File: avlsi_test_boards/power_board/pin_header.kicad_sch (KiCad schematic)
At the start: 3 parts, among them J5 Conn_01x02_Pin, J6 Conn_01x02_Pin

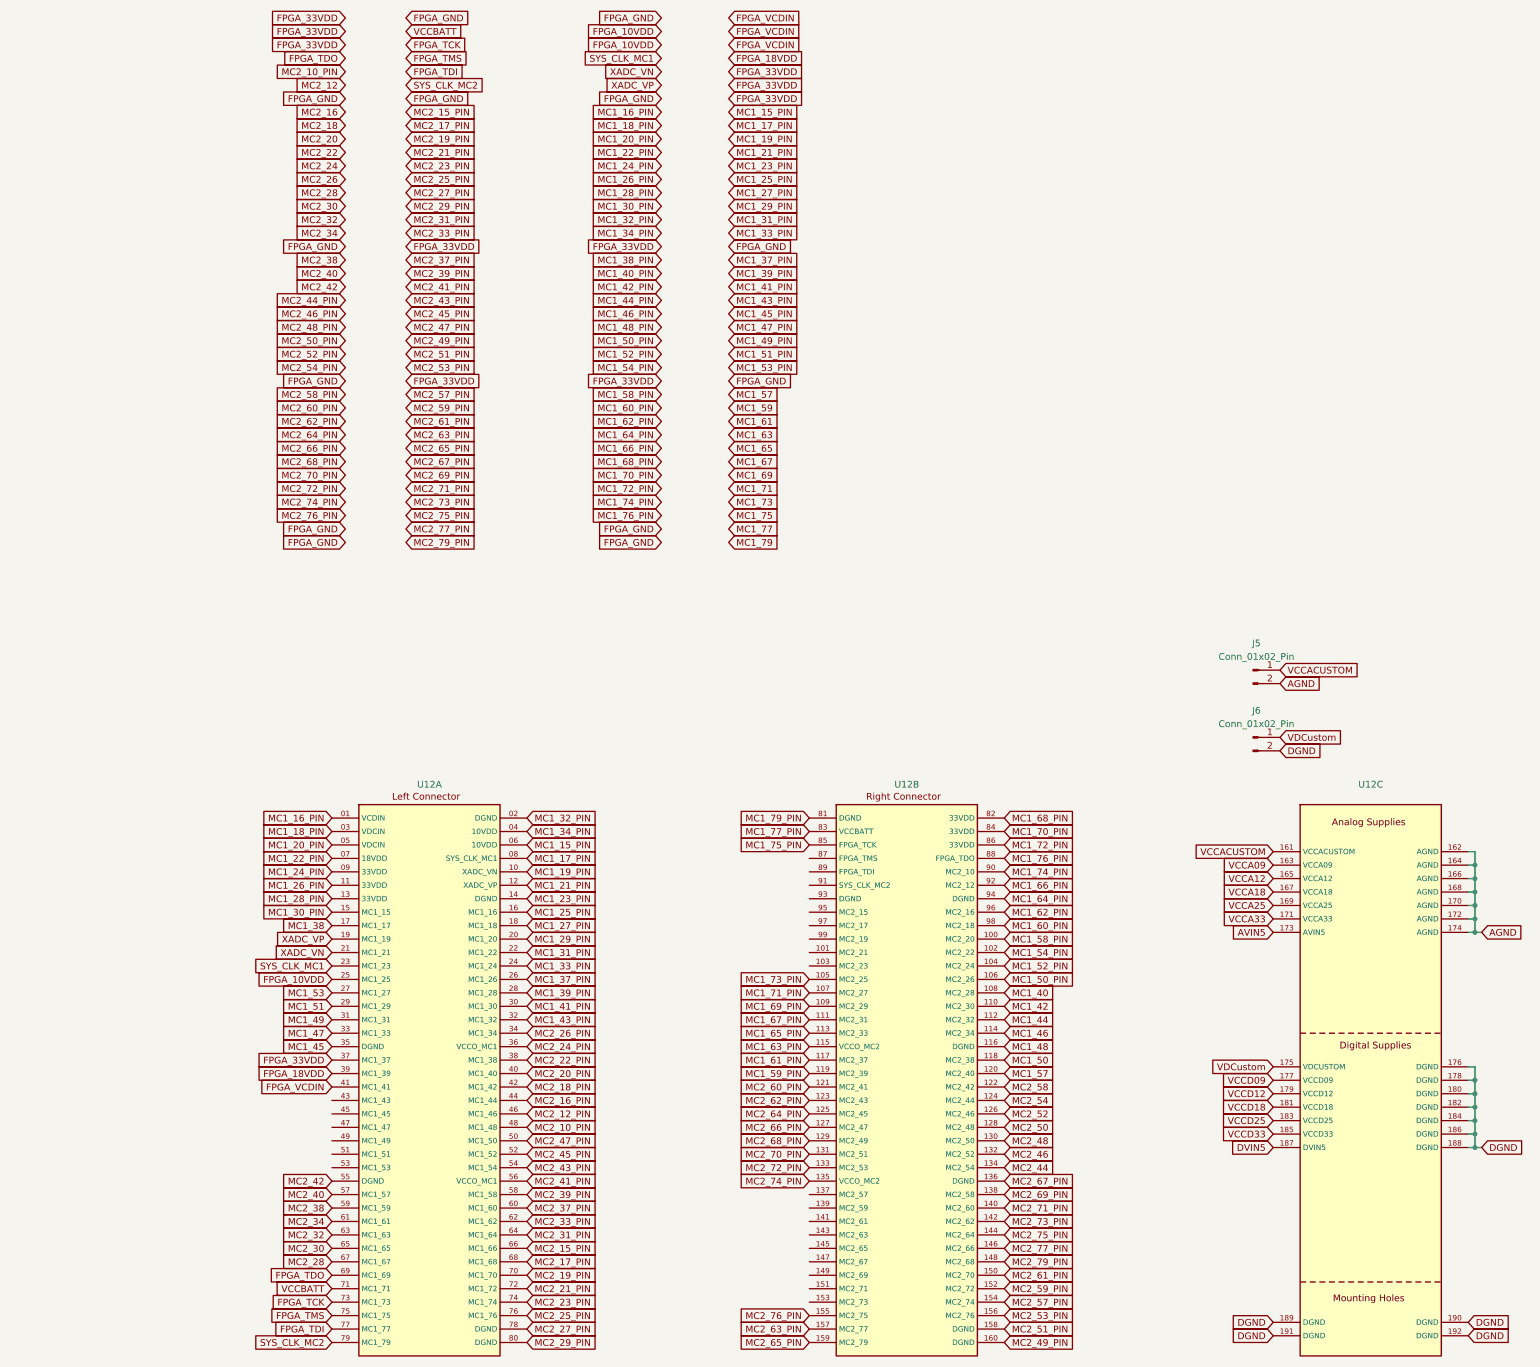
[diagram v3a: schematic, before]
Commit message: Add power board
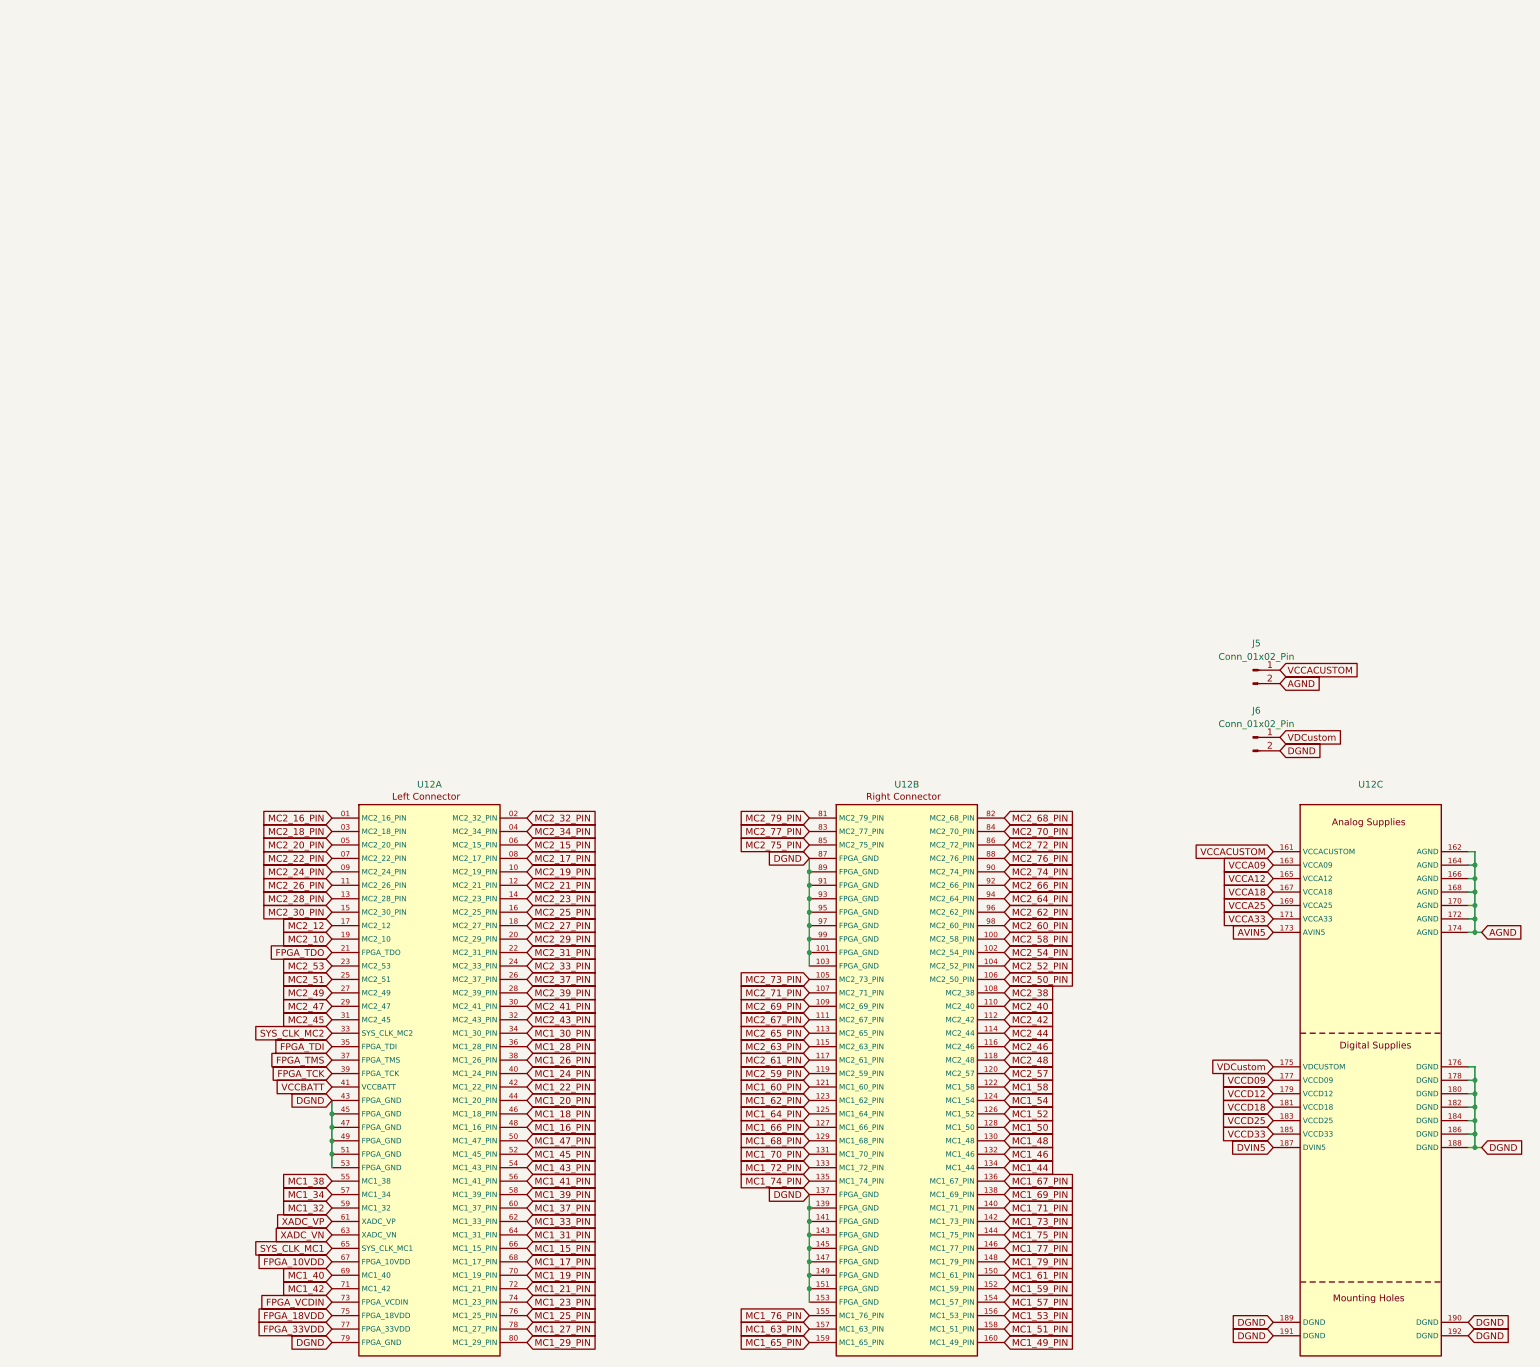
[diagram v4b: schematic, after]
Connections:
- net MC1_45 is gone; now on net FPGA_TDI: U12.35 (FPGA_TDI)
- net MC1_47 is gone; now on net SYS_CLK_MC2: U12.33 (SYS_CLK_MC2)
- net MC1_50_PIN is gone; now on net MC2_50_PIN: U12.106 (MC2_50_PIN)
- net MC1_52_PIN is gone; now on net MC2_52_PIN: U12.104 (MC2_52_PIN)
- net MC1_54_PIN is gone; now on net MC2_54_PIN: U12.102 (MC2_54_PIN)
- net MC1_58_PIN is gone; now on net MC2_58_PIN: U12.100 (MC2_58_PIN)
- net MC2_10_PIN is gone; now on net MC1_16_PIN: U12.48 (MC1_16_PIN)
- net MC2_12_PIN is gone; now on net MC1_18_PIN: U12.46 (MC1_18_PIN)
- net MC2_28 is gone; now on net FPGA_10VDD: U12.67 (FPGA_10VDD)
- net MC2_30 is gone; now on net SYS_CLK_MC1: U12.65 (SYS_CLK_MC1)
- net MC2_32 is gone; now on net XADC_VN: U12.63 (XADC_VN)
- net MC2_34 is gone; now on net XADC_VP: U12.61 (XADC_VP)
- net MC2_45_PIN is gone; now on net MC1_45_PIN: U12.52 (MC1_45_PIN)
- net MC2_47_PIN is gone; now on net MC1_47_PIN: U12.50 (MC1_47_PIN)
- net MC2_49_PIN is gone; now on net MC1_49_PIN: U12.160 (MC1_49_PIN)
- net MC2_50 is gone; now on net MC1_50: U12.128 (MC1_50)
- net MC2_51_PIN is gone; now on net MC1_51_PIN: U12.158 (MC1_51_PIN)
- net MC2_53_PIN is gone; now on net MC1_53_PIN: U12.156 (MC1_53_PIN)
- net DGND: now also U12.101 (FPGA_GND), U12.103 (FPGA_GND), U12.137 (FPGA_GND), U12.139 (FPGA_GND), U12.141 (FPGA_GND), U12.143 (FPGA_GND), U12.145 (FPGA_GND), U12.147 (FPGA_GND), U12.149 (FPGA_GND), U12.151 (FPGA_GND), U12.153 (FPGA_GND), U12.43 (FPGA_GND), U12.45 (FPGA_GND), U12.47 (FPGA_GND), U12.49 (FPGA_GND), U12.51 (FPGA_GND), U12.53 (FPGA_GND), U12.79 (FPGA_GND), U12.87 (FPGA_GND), U12.89 (FPGA_GND), U12.91 (FPGA_GND), U12.93 (FPGA_GND), U12.95 (FPGA_GND), U12.97 (FPGA_GND), U12.99 (FPGA_GND)
- net FPGA_10VDD: no longer U12.25 (MC1_25)
- net FPGA_18VDD: now also U12.75 (FPGA_18VDD); no longer U12.39 (MC1_39)
- net FPGA_33VDD: now also U12.77 (FPGA_33VDD); no longer U12.37 (MC1_37)
- net FPGA_TCK: now also U12.39 (FPGA_TCK); no longer U12.73 (MC1_73)
- net FPGA_TDI: no longer U12.77 (MC1_77)
- net FPGA_TDO: now also U12.21 (FPGA_TDO); no longer U12.69 (MC1_69)
- net FPGA_TMS: now also U12.37 (FPGA_TMS); no longer U12.75 (MC1_75)
- net FPGA_VCDIN: now also U12.73 (FPGA_VCDIN); no longer U12.41 (MC1_41)
- net MC1_15_PIN: now also U12.66 (MC1_15_PIN); no longer U12.06 (10VDD)
- net MC1_16_PIN: no longer U12.01 (VCDIN)
- net MC1_17_PIN: now also U12.68 (MC1_17_PIN); no longer U12.08 (SYS_CLK_MC1)
- net MC1_18_PIN: no longer U12.03 (VDCIN)
- net MC1_19_PIN: now also U12.70 (MC1_19_PIN); no longer U12.10 (XADC_VN)
- net MC1_20_PIN: now also U12.44 (MC1_20_PIN); no longer U12.05 (VDCIN)
- net MC1_21_PIN: now also U12.72 (MC1_21_PIN); no longer U12.12 (XADC_VP)
- net MC1_22_PIN: now also U12.42 (MC1_22_PIN); no longer U12.07 (18VDD)
- net MC1_23_PIN: now also U12.74 (MC1_23_PIN); no longer U12.14 (DGND)
- net MC1_24_PIN: now also U12.40 (MC1_24_PIN); no longer U12.09 (33VDD)
- net MC1_25_PIN: now also U12.76 (MC1_25_PIN); no longer U12.16 (MC1_16)
- net MC1_26_PIN: now also U12.38 (MC1_26_PIN); no longer U12.11 (33VDD)
- net MC1_27_PIN: now also U12.78 (MC1_27_PIN); no longer U12.18 (MC1_18)
- net MC1_28_PIN: now also U12.36 (MC1_28_PIN); no longer U12.13 (33VDD)
- net MC1_29_PIN: now also U12.80 (MC1_29_PIN); no longer U12.20 (MC1_20)
- net MC1_30_PIN: now also U12.34 (MC1_30_PIN); no longer U12.15 (MC1_15)
- net MC1_31_PIN: now also U12.64 (MC1_31_PIN); no longer U12.22 (MC1_22)
- net MC1_33_PIN: now also U12.62 (MC1_33_PIN); no longer U12.24 (MC1_24)
- net MC1_37_PIN: now also U12.60 (MC1_37_PIN); no longer U12.26 (MC1_26)
- net MC1_38: now also U12.55 (MC1_38); no longer U12.17 (MC1_17)
- net MC1_39_PIN: now also U12.58 (MC1_39_PIN); no longer U12.28 (MC1_28)
- net MC1_40: now also U12.69 (MC1_40); no longer U12.108 (MC2_28)
- net MC1_41_PIN: now also U12.56 (MC1_41_PIN); no longer U12.30 (MC1_30)
- net MC1_42: now also U12.71 (MC1_42); no longer U12.110 (MC2_30)
- net MC1_43_PIN: now also U12.54 (MC1_43_PIN); no longer U12.32 (MC1_32)
- net MC1_44: now also U12.134 (MC1_44); no longer U12.112 (MC2_32)
- net MC1_46: now also U12.132 (MC1_46); no longer U12.114 (MC2_34)
- net MC1_48: now also U12.130 (MC1_48); no longer U12.116 (DGND)
- net MC1_50: no longer U12.118 (MC2_38)
- net MC1_59_PIN: now also U12.152 (MC1_59_PIN); no longer U12.119 (MC2_39)
- net MC1_60_PIN: now also U12.121 (MC1_60_PIN); no longer U12.98 (MC2_18)
- net MC1_61_PIN: now also U12.150 (MC1_61_PIN); no longer U12.117 (MC2_37)
- net MC1_62_PIN: now also U12.123 (MC1_62_PIN); no longer U12.96 (MC2_16)
- net MC1_63_PIN: now also U12.157 (MC1_63_PIN); no longer U12.115 (VCCO_MC2)
- net MC1_64_PIN: now also U12.125 (MC1_64_PIN); no longer U12.94 (DGND)
- net MC1_65_PIN: now also U12.159 (MC1_65_PIN); no longer U12.113 (MC2_33)
- net MC1_66_PIN: now also U12.127 (MC1_66_PIN); no longer U12.92 (MC2_12)
- net MC1_67_PIN: now also U12.136 (MC1_67_PIN); no longer U12.111 (MC2_31)
- net MC1_68_PIN: now also U12.129 (MC1_68_PIN); no longer U12.82 (33VDD)
- net MC1_69_PIN: now also U12.138 (MC1_69_PIN); no longer U12.109 (MC2_29)
- net MC1_70_PIN: now also U12.131 (MC1_70_PIN); no longer U12.84 (33VDD)
- net MC1_71_PIN: now also U12.140 (MC1_71_PIN); no longer U12.107 (MC2_27)
- net MC1_72_PIN: now also U12.133 (MC1_72_PIN); no longer U12.86 (33VDD)
- net MC1_73_PIN: now also U12.142 (MC1_73_PIN); no longer U12.105 (MC2_25)
- net MC1_74_PIN: now also U12.135 (MC1_74_PIN); no longer U12.90 (MC2_10)
- net MC1_75_PIN: now also U12.144 (MC1_75_PIN); no longer U12.85 (FPGA_TCK)
- net MC1_76_PIN: now also U12.155 (MC1_76_PIN); no longer U12.88 (FPGA_TDO)
- net MC1_77_PIN: now also U12.146 (MC1_77_PIN); no longer U12.83 (VCCBATT)
- net MC1_79_PIN: now also U12.148 (MC1_79_PIN); no longer U12.81 (DGND)
- net MC2_12: now also U12.17 (MC2_12)
- net MC2_15_PIN: now also U12.06 (MC2_15_PIN); no longer U12.66 (MC1_66)
- net MC2_16_PIN: now also U12.01 (MC2_16_PIN); no longer U12.44 (MC1_44)
- net MC2_17_PIN: now also U12.08 (MC2_17_PIN); no longer U12.68 (MC1_68)
- net MC2_18_PIN: now also U12.03 (MC2_18_PIN); no longer U12.42 (MC1_42)
- net MC2_19_PIN: now also U12.10 (MC2_19_PIN); no longer U12.70 (MC1_70)
- net MC2_20_PIN: now also U12.05 (MC2_20_PIN); no longer U12.40 (MC1_40)
- net MC2_21_PIN: now also U12.12 (MC2_21_PIN); no longer U12.72 (MC1_72)
- net MC2_22_PIN: now also U12.07 (MC2_22_PIN); no longer U12.38 (MC1_38)
- net MC2_23_PIN: now also U12.14 (MC2_23_PIN); no longer U12.74 (MC1_74)
- net MC2_24_PIN: now also U12.09 (MC2_24_PIN); no longer U12.36 (VCCO_MC1)
- net MC2_25_PIN: now also U12.16 (MC2_25_PIN); no longer U12.76 (MC1_76)
- net MC2_26_PIN: now also U12.11 (MC2_26_PIN); no longer U12.34 (MC1_34)
- net MC2_27_PIN: now also U12.18 (MC2_27_PIN); no longer U12.78 (DGND)
- net MC2_29_PIN: now also U12.20 (MC2_29_PIN); no longer U12.80 (DGND)
- net MC2_31_PIN: now also U12.22 (MC2_31_PIN); no longer U12.64 (MC1_64)
- net MC2_33_PIN: now also U12.24 (MC2_33_PIN); no longer U12.62 (MC1_62)
- net MC2_37_PIN: now also U12.26 (MC2_37_PIN); no longer U12.60 (MC1_60)
- net MC2_38: now also U12.108 (MC2_38); no longer U12.59 (MC1_59)
- net MC2_39_PIN: now also U12.28 (MC2_39_PIN); no longer U12.58 (MC1_58)
- net MC2_40: now also U12.110 (MC2_40); no longer U12.57 (MC1_57)
- net MC2_41_PIN: now also U12.30 (MC2_41_PIN); no longer U12.56 (VCCO_MC1)
- net MC2_42: now also U12.112 (MC2_42); no longer U12.55 (DGND)
- net MC2_43_PIN: now also U12.32 (MC2_43_PIN); no longer U12.54 (MC1_54)
- net MC2_44: now also U12.114 (MC2_44); no longer U12.134 (MC2_54)
- net MC2_46: now also U12.116 (MC2_46); no longer U12.132 (MC2_52)
- net MC2_48: now also U12.118 (MC2_48); no longer U12.130 (MC2_50)
- net MC2_59_PIN: now also U12.119 (MC2_59_PIN); no longer U12.152 (MC2_72)
- net MC2_60_PIN: now also U12.98 (MC2_60_PIN); no longer U12.121 (MC2_41)
- net MC2_61_PIN: now also U12.117 (MC2_61_PIN); no longer U12.150 (MC2_70)
- net MC2_62_PIN: now also U12.96 (MC2_62_PIN); no longer U12.123 (MC2_43)
- net MC2_63_PIN: now also U12.115 (MC2_63_PIN); no longer U12.157 (MC2_77)
- net MC2_64_PIN: now also U12.94 (MC2_64_PIN); no longer U12.125 (MC2_45)
- net MC2_65_PIN: now also U12.113 (MC2_65_PIN); no longer U12.159 (MC2_79)
- net MC2_66_PIN: now also U12.92 (MC2_66_PIN); no longer U12.127 (MC2_47)
- net MC2_67_PIN: now also U12.111 (MC2_67_PIN); no longer U12.136 (DGND)
- net MC2_68_PIN: now also U12.82 (MC2_68_PIN); no longer U12.129 (MC2_49)
- net MC2_69_PIN: now also U12.109 (MC2_69_PIN); no longer U12.138 (MC2_58)
- net MC2_70_PIN: now also U12.84 (MC2_70_PIN); no longer U12.131 (MC2_51)
- net MC2_71_PIN: now also U12.107 (MC2_71_PIN); no longer U12.140 (MC2_60)
- net MC2_72_PIN: now also U12.86 (MC2_72_PIN); no longer U12.133 (MC2_53)
- net MC2_73_PIN: now also U12.105 (MC2_73_PIN); no longer U12.142 (MC2_62)
- net MC2_74_PIN: now also U12.90 (MC2_74_PIN); no longer U12.135 (VCCO_MC2)
- net MC2_75_PIN: now also U12.85 (MC2_75_PIN); no longer U12.144 (MC2_64)
- net MC2_76_PIN: now also U12.88 (MC2_76_PIN); no longer U12.155 (MC2_75)
- net MC2_77_PIN: now also U12.83 (MC2_77_PIN); no longer U12.146 (MC2_66)
- net MC2_79_PIN: now also U12.81 (MC2_79_PIN); no longer U12.148 (MC2_68)
- net SYS_CLK_MC1: no longer U12.23 (MC1_23)
- net SYS_CLK_MC2: no longer U12.79 (MC1_79)
- net VCCBATT: now also U12.41 (VCCBATT); no longer U12.71 (MC1_71)
- net XADC_VN: no longer U12.21 (MC1_21)
- net XADC_VP: no longer U12.19 (MC1_19)
- net MC1_32_PIN renamed MC2_32_PIN
- net MC1_34_PIN renamed MC2_34_PIN
- net MC1_49 renamed MC2_45
- net MC1_51 renamed MC2_47
- net MC1_53 renamed MC2_49
- net MC1_57 renamed MC2_57
- net MC2_52 renamed MC1_52
- net MC2_54 renamed MC1_54
- net MC2_57_PIN renamed MC1_57_PIN
- net MC2_58 renamed MC1_58
- new net MC1_32: U12.59 (MC1_32)
- new net MC1_34: U12.57 (MC1_34)
- new net MC2_10: U12.19 (MC2_10)
- new net MC2_28_PIN: U12.13 (MC2_28_PIN)
- new net MC2_30_PIN: U12.15 (MC2_30_PIN)
- new net MC2_51: U12.25 (MC2_51)
- new net MC2_53: U12.23 (MC2_53)
